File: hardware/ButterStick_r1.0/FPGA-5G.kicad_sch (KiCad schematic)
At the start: 1 part, among them U4 ECP5UM5G_85_CABGA381

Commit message: hw.r1d0: Review complete, gerbers generated
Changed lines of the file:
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@@
 (kicad_sch (version 20200618) (host eeschema "5.99.0-unknown-73168a9~101~ubuntu18.04.1")
-  (page 11 18)
+  (page 1 18)
   (paper "A4")
   (title_block
     (title "ButterStick")
-    (date "2020-07-16")
+    (date "2020-07-17")
     (rev "r1.0")
     (company "GsD")
     (comment 1 "Functional prototyping board for the Lattice ECP5.")
   )
+  (no_connect (at 119.38 134.62))
   (no_connect (at 119.38 132.08))
-  (no_connect (at 119.38 134.62))
   (bus_entry (at 90.17 67.31) (size 2.54 -2.54)
     (stroke (width 0.1524) (type solid) (color 0 0 0 0))
@@
     (stroke (width 0) (type solid) (color 0 0 0 0))
   )
-  (bus (pts (xy 90.17 67.31) (xy 90.17 69.85))
+  (bus (pts (xy 90.17 67.31) (xy 90.17 72.39))
     (stroke (width 0) (type solid) (color 0 0 0 0))
   )
-  (bus (pts (xy 90.17 69.85) (xy 90.17 74.93))
+  (bus (pts (xy 90.17 72.39) (xy 90.17 80.01))
     (stroke (width 0) (type solid) (color 0 0 0 0))
   )
-  (bus (pts (xy 90.17 74.93) (xy 90.17 82.55))
+  (bus (pts (xy 90.17 80.01) (xy 90.17 82.55))
     (stroke (width 0) (type solid) (color 0 0 0 0))
   )
@@
     (stroke (width 0) (type solid) (color 0 0 0 0))
   )
-  (bus (pts (xy 90.17 87.63) (xy 90.17 92.71))
+  (bus (pts (xy 90.17 87.63) (xy 90.17 95.25))
     (stroke (width 0) (type solid) (color 0 0 0 0))
   )
-  (bus (pts (xy 90.17 92.71) (xy 90.17 109.22))
+  (bus (pts (xy 90.17 95.25) (xy 90.17 111.76))
     (stroke (width 0) (type solid) (color 0 0 0 0))
   )
-  (bus (pts (xy 90.17 109.22) (xy 90.17 114.3))
+  (bus (pts (xy 90.17 111.76) (xy 90.17 116.84))
     (stroke (width 0) (type solid) (color 0 0 0 0))
   )
-  (bus (pts (xy 90.17 114.3) (xy 90.17 121.92))
+  (bus (pts (xy 90.17 116.84) (xy 90.17 121.92))
     (stroke (width 0) (type solid) (color 0 0 0 0))
   )

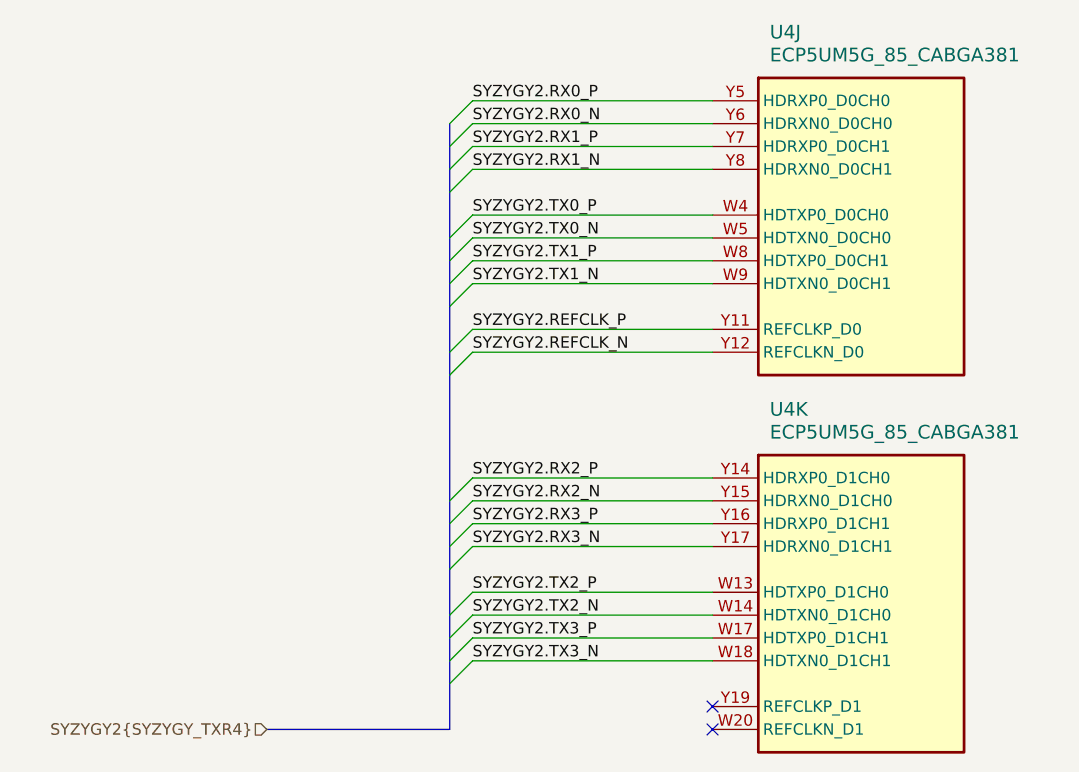
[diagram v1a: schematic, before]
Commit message: hw.r1d0: Update BOM fieids in schematic.
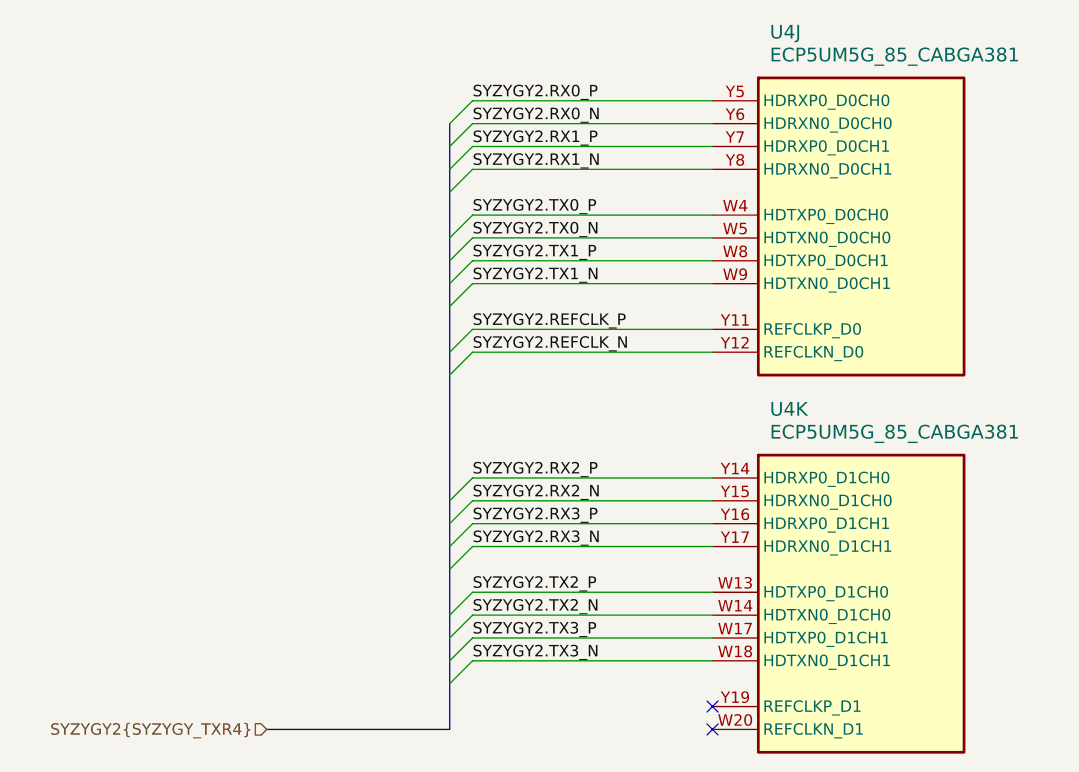
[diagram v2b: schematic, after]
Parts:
- U4: Mfg (none) -> Lattice Semiconductor Corporation; PN (none) -> LFE5UM5G-85F-8BG381C; manf# ECP5UM5G_85 -> (none)
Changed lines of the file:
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@@
     (comment 1 "Functional prototyping board for the Lattice ECP5.")
   )
+  (no_connect (at 119.38 132.08))
   (no_connect (at 119.38 134.62))
-  (no_connect (at 119.38 132.08))
   (bus_entry (at 90.17 67.31) (size 2.54 -2.54)
     (stroke (width 0.1524) (type solid) (color 0 0 0 0))
@@
     (stroke (width 0) (type solid) (color 0 0 0 0))
   )
-  (bus (pts (xy 90.17 80.01) (xy 90.17 82.55))
-    (stroke (width 0) (type solid) (color 0 0 0 0))
-  )
-  (bus (pts (xy 90.17 82.55) (xy 90.17 87.63))
-    (stroke (width 0) (type solid) (color 0 0 0 0))
-  )
-  (bus (pts (xy 90.17 87.63) (xy 90.17 95.25))
-    (stroke (width 0) (type solid) (color 0 0 0 0))
-  )
-  (bus (pts (xy 90.17 95.25) (xy 90.17 111.76))
-    (stroke (width 0) (type solid) (color 0 0 0 0))
-  )
-  (bus (pts (xy 90.17 111.76) (xy 90.17 116.84))
-    (stroke (width 0) (type solid) (color 0 0 0 0))
-  )
-  (bus (pts (xy 90.17 116.84) (xy 90.17 121.92))
+  (bus (pts (xy 90.17 80.01) (xy 90.17 85.09))
+    (stroke (width 0) (type solid) (color 0 0 0 0))
+  )
+  (bus (pts (xy 90.17 85.09) (xy 90.17 92.71))
+    (stroke (width 0) (type solid) (color 0 0 0 0))
+  )
+  (bus (pts (xy 90.17 92.71) (xy 90.17 109.22))
+    (stroke (width 0) (type solid) (color 0 0 0 0))
+  )
+  (bus (pts (xy 90.17 109.22) (xy 90.17 114.3))
+    (stroke (width 0) (type solid) (color 0 0 0 0))
+  )
+  (bus (pts (xy 90.17 114.3) (xy 90.17 121.92))
     (stroke (width 0) (type solid) (color 0 0 0 0))
   )
@@
       (effects (font (size 1.524 1.524)) (justify right) hide)
     )
-    (property "manf#" "ECP5UM5G_85" (id 4) (at 123.19 68.58 0)
-      (effects (font (size 1.524 1.524)) (justify right) hide)
+    (property "manf#" "" (id 4) (at 123.19 68.58 0)
+      (effects (font (size 1.524 1.524)) (justify right) hide)
+    )
+    (property "Mfg" "Lattice Semiconductor Corporation" (id 4) (at 119.38 67.31 0)
+      (effects (font (size 1.27 1.27)) hide)
+    )
+    (property "PN" "LFE5UM5G-85F-8BG381C" (id 5) (at 119.38 67.31 0)
+      (effects (font (size 1.27 1.27)) hide)
     )
   )
@@
       (effects (font (size 1.524 1.524)) (justify right) hide)
     )
-    (property "manf#" "ECP5UM5G_85" (id 4) (at 123.19 110.49 0)
-      (effects (font (size 1.524 1.524)) (justify right) hide)
-    )
-  )
+    (property "manf#" "" (id 4) (at 123.19 110.49 0)
+      (effects (font (size 1.524 1.524)) (justify right) hide)
+    )
+    (property "Mfg" "Lattice Semiconductor Corporation" (id 4) (at 119.38 109.22 0)
+      (effects (font (size 1.27 1.27)) hide)
+    )
+    (property "PN" "LFE5UM5G-85F-8BG381C" (id 5) (at 119.38 109.22 0)
+      (effects (font (size 1.27 1.27)) hide)
+    )
+  )

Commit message: hw.r1d0: Fix RGMII straps
This commit correctly sets the stop resistos on the RGMII lines to 1K5
instead of DNP.
Also regenerate and add a schematic in PDF format.

Fixes #6
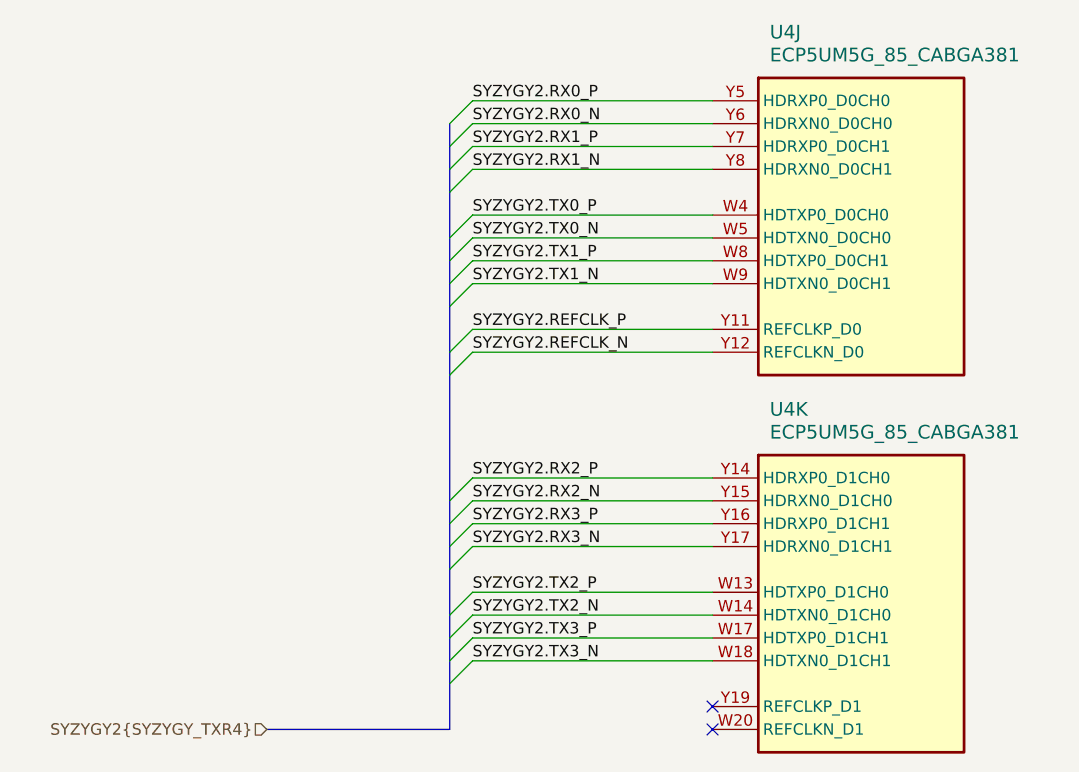
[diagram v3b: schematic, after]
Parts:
- U4: PN LFE5UM5G-85F-8BG381C -> LFE5UM5G-85F-8BG381I
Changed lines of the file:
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@@
-(kicad_sch (version 20200618) (host eeschema "5.99.0-unknown-73168a9~101~ubuntu18.04.1")
+(kicad_sch (version 20201015) (generator eeschema)
   (page 1 18)
   (paper "A4")
   (title_block
     (title "ButterStick")
-    (date "2020-07-17")
+    (date "2020-11-01")
     (rev "r1.0")
     (company "GsD")
     (comment 1 "Functional prototyping board for the Lattice ECP5.")
+    (comment 2 "SYZYGY compatible")
   )
   (no_connect (at 119.38 132.08))
@@
     (stroke (width 0) (type solid) (color 0 0 0 0))
   )
-  (bus (pts (xy 90.17 67.31) (xy 90.17 72.39))
-    (stroke (width 0) (type solid) (color 0 0 0 0))
-  )
-  (bus (pts (xy 90.17 72.39) (xy 90.17 80.01))
-    (stroke (width 0) (type solid) (color 0 0 0 0))
-  )
-  (bus (pts (xy 90.17 80.01) (xy 90.17 85.09))
-    (stroke (width 0) (type solid) (color 0 0 0 0))
-  )
-  (bus (pts (xy 90.17 85.09) (xy 90.17 92.71))
-    (stroke (width 0) (type solid) (color 0 0 0 0))
-  )
-  (bus (pts (xy 90.17 92.71) (xy 90.17 109.22))
-    (stroke (width 0) (type solid) (color 0 0 0 0))
-  )
-  (bus (pts (xy 90.17 109.22) (xy 90.17 114.3))
-    (stroke (width 0) (type solid) (color 0 0 0 0))
-  )
-  (bus (pts (xy 90.17 114.3) (xy 90.17 121.92))
-    (stroke (width 0) (type solid) (color 0 0 0 0))
-  )
-  (bus (pts (xy 90.17 121.92) (xy 90.17 127))
-    (stroke (width 0) (type solid) (color 0 0 0 0))
-  )
-  (bus (pts (xy 90.17 127) (xy 90.17 134.62))
+  (bus (pts (xy 90.17 67.31) (xy 90.17 69.85))
+    (stroke (width 0) (type solid) (color 0 0 0 0))
+  )
+  (bus (pts (xy 90.17 69.85) (xy 90.17 72.39))
+    (stroke (width 0) (type solid) (color 0 0 0 0))
+  )
+  (bus (pts (xy 90.17 72.39) (xy 90.17 74.93))
+    (stroke (width 0) (type solid) (color 0 0 0 0))
+  )
+  (bus (pts (xy 90.17 74.93) (xy 90.17 80.01))
+    (stroke (width 0) (type solid) (color 0 0 0 0))
+  )
+  (bus (pts (xy 90.17 80.01) (xy 90.17 82.55))
+    (stroke (width 0) (type solid) (color 0 0 0 0))
+  )
+  (bus (pts (xy 90.17 82.55) (xy 90.17 85.09))
+    (stroke (width 0) (type solid) (color 0 0 0 0))
+  )
+  (bus (pts (xy 90.17 85.09) (xy 90.17 87.63))
+    (stroke (width 0) (type solid) (color 0 0 0 0))
+  )
+  (bus (pts (xy 90.17 87.63) (xy 90.17 92.71))
+    (stroke (width 0) (type solid) (color 0 0 0 0))
+  )
+  (bus (pts (xy 90.17 92.71) (xy 90.17 95.25))
+    (stroke (width 0) (type solid) (color 0 0 0 0))
+  )
+  (bus (pts (xy 90.17 95.25) (xy 90.17 109.22))
+    (stroke (width 0) (type solid) (color 0 0 0 0))
+  )
+  (bus (pts (xy 90.17 109.22) (xy 90.17 111.76))
+    (stroke (width 0) (type solid) (color 0 0 0 0))
+  )
+  (bus (pts (xy 90.17 111.76) (xy 90.17 114.3))
+    (stroke (width 0) (type solid) (color 0 0 0 0))
+  )
+  (bus (pts (xy 90.17 114.3) (xy 90.17 116.84))
+    (stroke (width 0) (type solid) (color 0 0 0 0))
+  )
+  (bus (pts (xy 90.17 116.84) (xy 90.17 121.92))
+    (stroke (width 0) (type solid) (color 0 0 0 0))
+  )
+  (bus (pts (xy 90.17 121.92) (xy 90.17 124.46))
+    (stroke (width 0) (type solid) (color 0 0 0 0))
+  )
+  (bus (pts (xy 90.17 124.46) (xy 90.17 127))
+    (stroke (width 0) (type solid) (color 0 0 0 0))
+  )
+  (bus (pts (xy 90.17 127) (xy 90.17 129.54))
+    (stroke (width 0) (type solid) (color 0 0 0 0))
+  )
+  (bus (pts (xy 90.17 129.54) (xy 90.17 134.62))
     (stroke (width 0) (type solid) (color 0 0 0 0))
   )
@@
       (effects (font (size 1.524 1.524)) (justify right) hide)
     )
+    (property "PN" "LFE5UM5G-85F-8BG381I" (id 5) (at 119.38 67.31 0)
+      (effects (font (size 1.27 1.27)) hide)
+    )
     (property "Mfg" "Lattice Semiconductor Corporation" (id 4) (at 119.38 67.31 0)
-      (effects (font (size 1.27 1.27)) hide)
-    )
-    (property "PN" "LFE5UM5G-85F-8BG381C" (id 5) (at 119.38 67.31 0)
       (effects (font (size 1.27 1.27)) hide)
     )
@@
       (effects (font (size 1.524 1.524)) (justify right) hide)
     )
+    (property "PN" "LFE5UM5G-85F-8BG381I" (id 5) (at 119.38 109.22 0)
+      (effects (font (size 1.27 1.27)) hide)
+    )
     (property "Mfg" "Lattice Semiconductor Corporation" (id 4) (at 119.38 109.22 0)
       (effects (font (size 1.27 1.27)) hide)
     )
-    (property "PN" "LFE5UM5G-85F-8BG381C" (id 5) (at 119.38 109.22 0)
-      (effects (font (size 1.27 1.27)) hide)
-    )
